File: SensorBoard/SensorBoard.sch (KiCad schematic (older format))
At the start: 16 parts

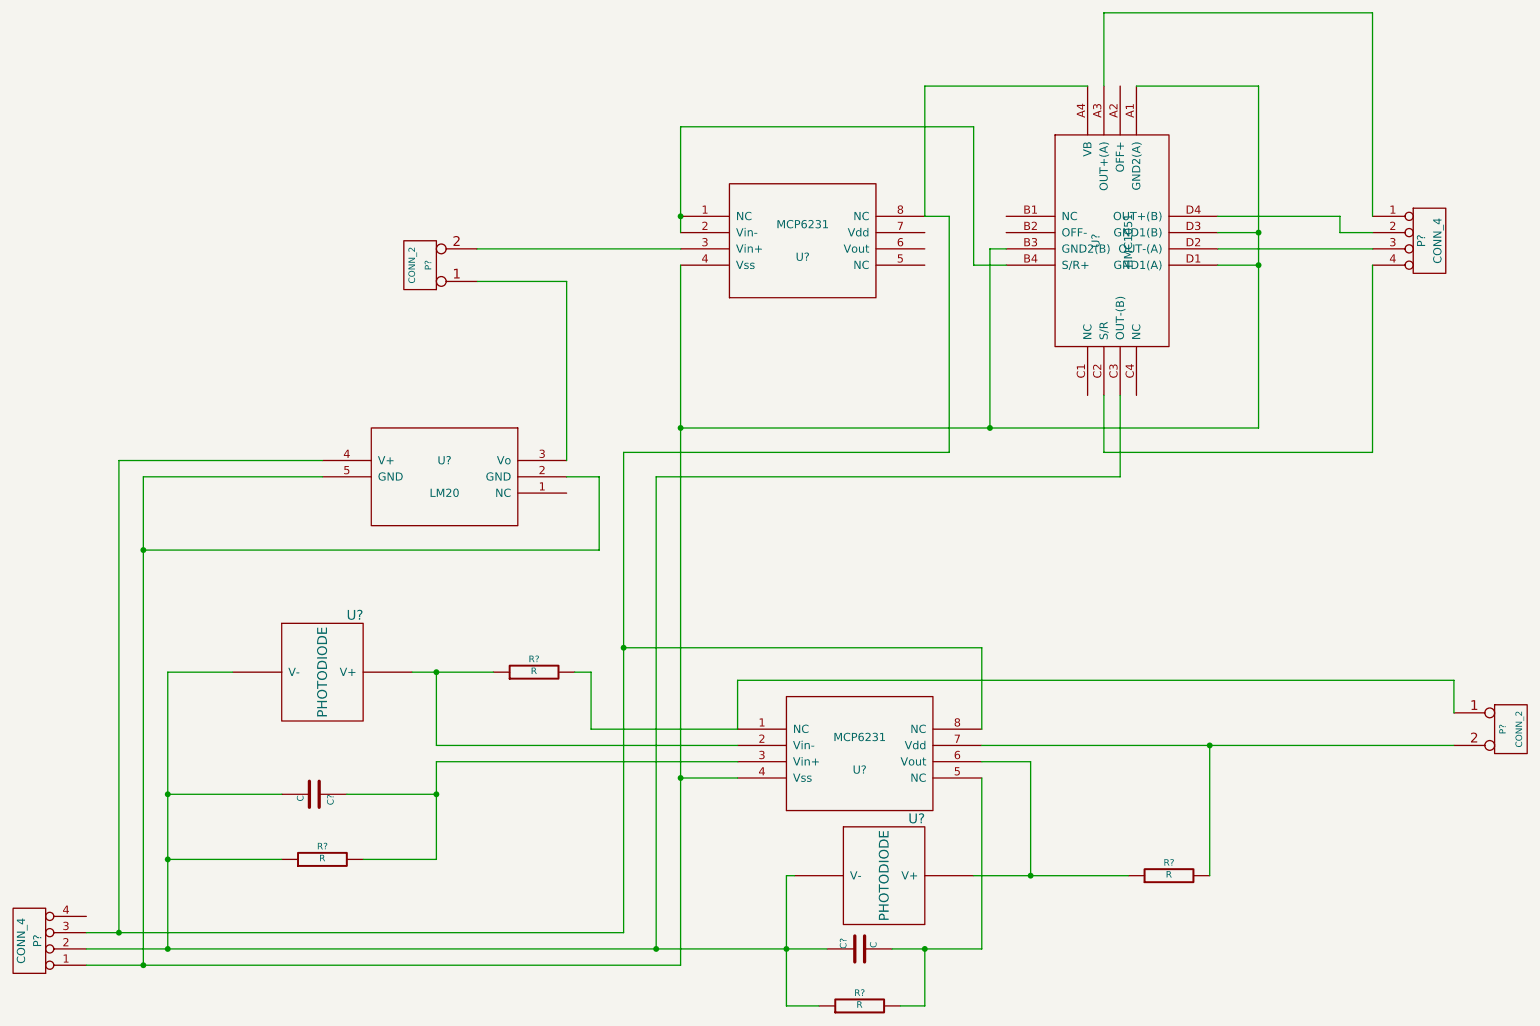
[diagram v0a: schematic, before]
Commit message: add label to everything on sensor board
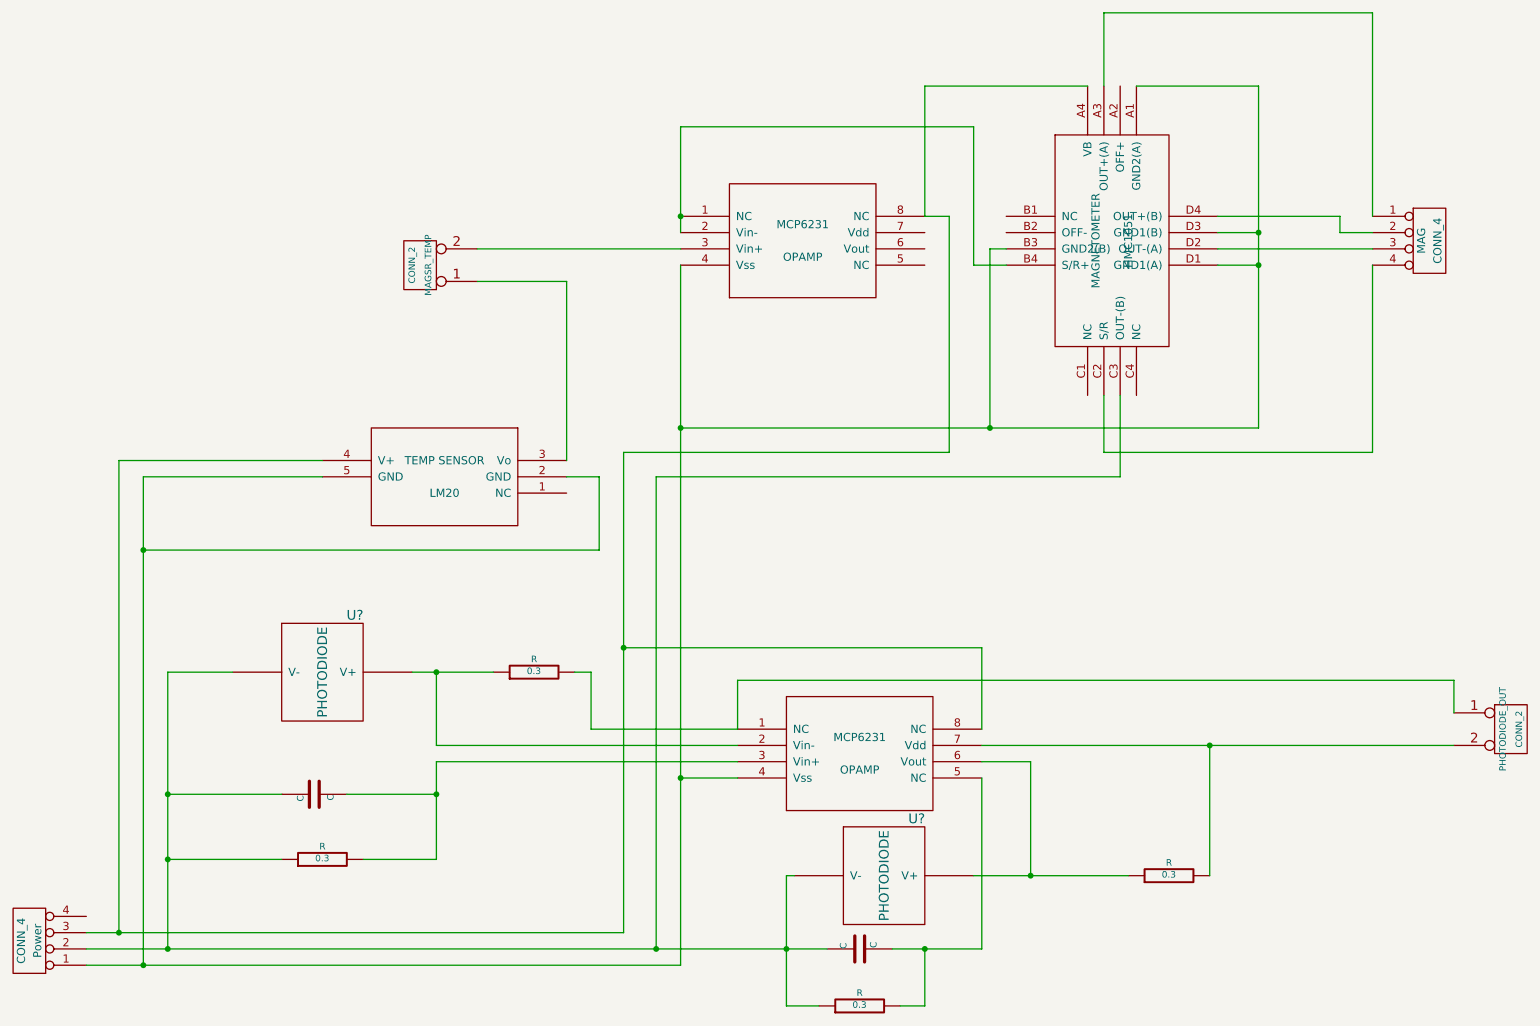
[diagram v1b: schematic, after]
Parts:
- R: renamed from R?; value R -> 0.3
- gave numbers to parts that had none: 8
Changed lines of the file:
@@
 $EndDescr
 $Comp
-L MCP6231 U?
+L MCP6231 OPAMP
 U 1 1 55529383
 P 6000 2700
-F 0 "U?" H 6000 2600 50  0000 C CNN
+F 0 "OPAMP" H 6000 2600 50  0000 C CNN
 F 1 "MCP6231" H 6000 2800 50  0000 C CNN
 F 2 "MODULE" H 6000 2700 50  0001 C CNN
@@
 $EndComp
 $Comp
-L CONN_4 P?
+L CONN_4 MAG
 U 1 1 555293ED
 P 9850 2700
-F 0 "P?" V 9800 2700 50  0000 C CNN
+F 0 "MAG" V 9800 2700 50  0000 C CNN
 F 1 "CONN_4" V 9900 2700 50  0000 C CNN
 F 2 "" H 9850 2700 60  0000 C CNN
@@
 $EndComp
 $Comp
-L CONN_2 P?
+L CONN_2 MAGSR_TEMP
 U 1 1 5552AB33
 P 3650 2850
-F 0 "P?" V 3600 2850 40  0000 C CNN
+F 0 "MAGSR_TEMP" V 3600 2850 40  0000 C CNN
 F 1 "CONN_2" V 3700 2850 40  0000 C CNN
 F 2 "" H 3650 2850 60  0000 C CNN
@@
 $EndComp
 $Comp
-L CONN_4 P?
+L CONN_4 Power
 U 1 1 5552AB45
 P 1250 7000
-F 0 "P?" V 1200 7000 50  0000 C CNN
+F 0 "Power" V 1200 7000 50  0000 C CNN
 F 1 "CONN_4" V 1300 7000 50  0000 C CNN
 F 2 "" H 1250 7000 60  0000 C CNN
@@
 $EndComp
 $Comp
-L LM20 U?
+L LM20 TEMP
 U 1 1 5552ACD4
 P 3800 4150
-F 0 "U?" H 3800 4050 50  0000 C CNN
+F 0 "TEMP SENSOR" H 3800 4050 50  0000 C CNN
 F 1 "LM20" H 3800 4250 50  0000 C CNN
 F 2 "MODULE" H 3800 4150 50  0001 C CNN
@@
 $EndComp
 $Comp
-L CONN_2 P?
+L CONN_2 PHOTODIODE_OUT
 U 1 1 5552ACE9
 P 10350 5700
-F 0 "P?" V 10300 5700 40  0000 C CNN
+F 0 "PHOTODIODE_OUT" V 10300 5700 40  0000 C CNN
 F 1 "CONN_2" V 10400 5700 40  0000 C CNN
 F 2 "" H 10350 5700 60  0000 C CNN
@@
 $EndComp
 $Comp
-L MCP6231 U?
+L MCP6231 OPAMP
 U 1 1 5552AD10
 P 6350 5850
-F 0 "U?" H 6350 5750 50  0000 C CNN
+F 0 "OPAMP" H 6350 5750 50  0000 C CNN
 F 1 "MCP6231" H 6350 5950 50  0000 C CNN
 F 2 "MODULE" H 6350 5850 50  0001 C CNN
@@
 $EndComp
 $Comp
-L C C?
+L C C
 U 1 1 5552AD2C
 P 6350 7050
-F 0 "C?" H 6350 7150 40  0000 L CNN
+F 0 "C" H 6350 7150 40  0000 L CNN
 F 1 "C" H 6356 6965 40  0000 L CNN
 F 2 "~" H 6388 6900 30  0000 C CNN
@@
 $EndComp
 $Comp
-L C C?
+L C C
 U 1 1 5552AD39
 P 3000 6100
-F 0 "C?" H 3000 6200 40  0000 L CNN
+F 0 "C" H 3000 6200 40  0000 L CNN
 F 1 "C" H 3006 6015 40  0000 L CNN
 F 2 "~" H 3038 5950 30  0000 C CNN
@@
 $EndComp
 $Comp
-L R R?
+L R R
 U 1 1 5552AD43
 P 3050 6500
-F 0 "R?" V 3130 6500 40  0000 C CNN
-F 1 "R" V 3057 6501 40  0000 C CNN
+F 0 "R" V 3130 6500 40  0000 C CNN
+F 1 "0.3" V 3057 6501 40  0000 C CNN
 F 2 "~" V 2980 6500 30  0000 C CNN
 F 3 "~" H 3050 6500 30  0000 C CNN
@@
 $EndComp
 $Comp
-L R R?
+L R R
 U 1 1 5552AD50
 P 6350 7400
-F 0 "R?" V 6430 7400 40  0000 C CNN
-F 1 "R" V 6357 7401 40  0000 C CNN
+F 0 "R" V 6430 7400 40  0000 C CNN
+F 1 "0.3" V 6357 7401 40  0000 C CNN
 F 2 "~" V 6280 7400 30  0000 C CNN
 F 3 "~" H 6350 7400 30  0000 C CNN
@@
 $EndComp
 $Comp
-L R R?
+L R R
 U 1 1 5552AD56
 P 8250 6600
-F 0 "R?" V 8330 6600 40  0000 C CNN
-F 1 "R" V 8257 6601 40  0000 C CNN
+F 0 "R" V 8330 6600 40  0000 C CNN
+F 1 "0.3" V 8257 6601 40  0000 C CNN
 F 2 "~" V 8180 6600 30  0000 C CNN
 F 3 "~" H 8250 6600 30  0000 C CNN
@@
 $EndComp
 $Comp
-L R R?
+L R R
 U 1 1 5552AD5C
 P 4350 5350
-F 0 "R?" V 4430 5350 40  0000 C CNN
-F 1 "R" V 4357 5351 40  0000 C CNN
+F 0 "R" V 4430 5350 40  0000 C CNN
+F 1 "0.3" V 4357 5351 40  0000 C CNN
 F 2 "~" V 4280 5350 30  0000 C CNN
 F 3 "~" H 4350 5350 30  0000 C CNN
@@
 $EndComp
 $Comp
-L HMC1051 U?
+L HMC1051 MAGNETOMETER
 U 1 1 555409A7
 P 7900 2700
-F 0 "U?" H 7900 2600 50  0000 C CNN
+F 0 "MAGNETOMETER" H 7900 2600 50  0000 C CNN
 F 1 "HMC1051" H 7900 2800 50  0000 C CNN
 F 2 "MODULE" H 7900 2700 50  0001 C CNN
